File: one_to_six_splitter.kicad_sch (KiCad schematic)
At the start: 0 parts

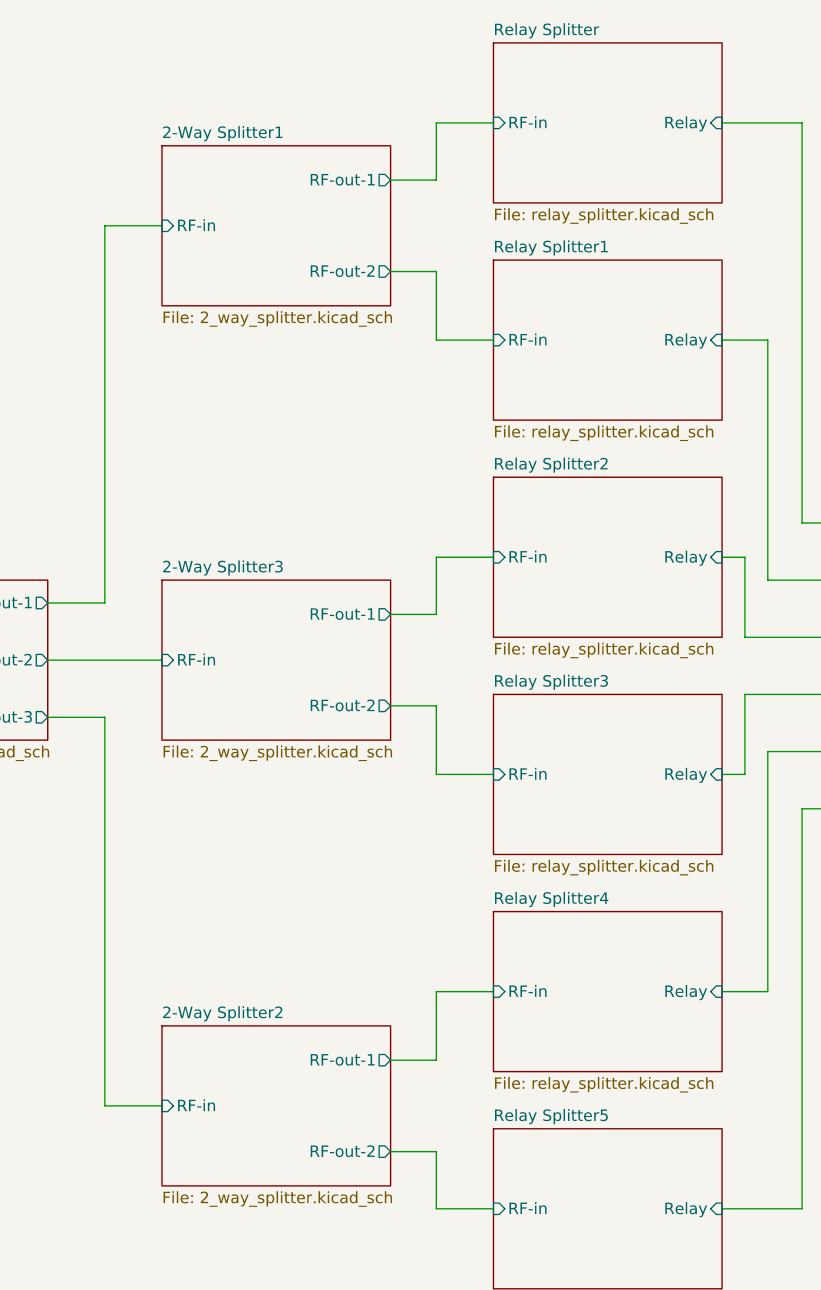
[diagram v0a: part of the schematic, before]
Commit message: changed to 1 to 6
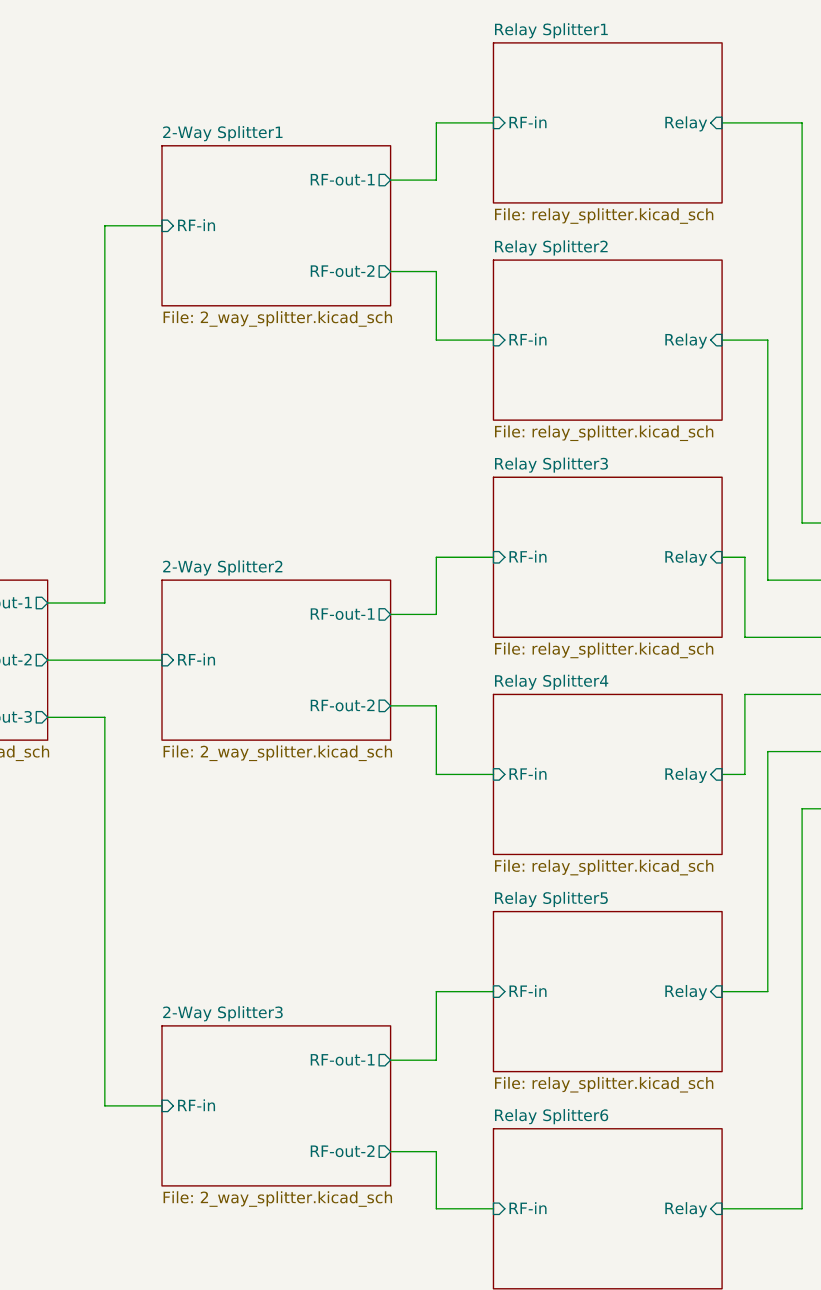
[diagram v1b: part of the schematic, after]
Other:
- removed sheet Relay Splitter
- added sheet Relay Splitter6 (relay_splitter.kicad_sch)
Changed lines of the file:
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@@
     (stroke (width 0.1524) (type solid) (color 0 0 0 0))
     (fill (color 0 0 0 0.0000))
-    (property "Sheet name" "Relay Splitter4" (id 0) (at 140.97 119.9384 0)
+    (property "Sheet name" "Relay Splitter5" (id 0) (at 140.97 119.9384 0)
       (effects (font (size 1.27 1.27)) (justify left bottom))
     )
@@
     (stroke (width 0.1524) (type solid) (color 0 0 0 0))
     (fill (color 0 0 0 0.0000))
-    (property "Sheet name" "Relay Splitter5" (id 0) (at 140.97 144.0684 0)
+    (property "Sheet name" "Relay Splitter6" (id 0) (at 140.97 144.0684 0)
       (effects (font (size 1.27 1.27)) (justify left bottom))
     )
@@
     (stroke (width 0.1524) (type solid) (color 0 0 0 0))
     (fill (color 0 0 0 0.0000))
-    (property "Sheet name" "Relay Splitter3" (id 0) (at 140.97 95.8084 0)
+    (property "Sheet name" "Relay Splitter4" (id 0) (at 140.97 95.8084 0)
       (effects (font (size 1.27 1.27)) (justify left bottom))
     )
@@
     (stroke (width 0.1524) (type solid) (color 0 0 0 0))
     (fill (color 0 0 0 0.0000))
-    (property "Sheet name" "Relay Splitter" (id 0) (at 140.97 23.4184 0)
+    (property "Sheet name" "Relay Splitter1" (id 0) (at 140.97 23.4184 0)
       (effects (font (size 1.27 1.27)) (justify left bottom))
     )
@@
     (stroke (width 0.1524) (type solid) (color 0 0 0 0))
     (fill (color 0 0 0 0.0000))
-    (property "Sheet name" "2-Way Splitter2" (id 0) (at 104.14 132.6384 0)
+    (property "Sheet name" "2-Way Splitter3" (id 0) (at 104.14 132.6384 0)
       (effects (font (size 1.27 1.27)) (justify left bottom))
     )
@@
     (stroke (width 0.1524) (type solid) (color 0 0 0 0))
     (fill (color 0 0 0 0.0000))
-    (property "Sheet name" "2-Way Splitter3" (id 0) (at 104.14 83.1084 0)
+    (property "Sheet name" "2-Way Splitter2" (id 0) (at 104.14 83.1084 0)
       (effects (font (size 1.27 1.27)) (justify left bottom))
     )
@@
     (stroke (width 0.1524) (type solid) (color 0 0 0 0))
     (fill (color 0 0 0 0.0000))
-    (property "Sheet name" "Relay Splitter1" (id 0) (at 140.97 47.5484 0)
+    (property "Sheet name" "Relay Splitter2" (id 0) (at 140.97 47.5484 0)
       (effects (font (size 1.27 1.27)) (justify left bottom))
     )
@@
     (stroke (width 0.1524) (type solid) (color 0 0 0 0))
     (fill (color 0 0 0 0.0000))
-    (property "Sheet name" "Relay Splitter2" (id 0) (at 140.97 71.6784 0)
+    (property "Sheet name" "Relay Splitter3" (id 0) (at 140.97 71.6784 0)
       (effects (font (size 1.27 1.27)) (justify left bottom))
     )

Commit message: pcb routed and made gerbers
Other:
- sheet Connectors ports: added RF-1, RF-2, RF-3, RF-4, RF-5, RF-6; removed none
- sheet Relay Splitter1 ports: added RF-out; removed none
- sheet Relay Splitter2 ports: added RF-out; removed none
- sheet Relay Splitter3 ports: added RF-out; removed none
- sheet Relay Splitter4 ports: added RF-out; removed none
- sheet Relay Splitter5 ports: added RF-out; removed none
- sheet Relay Splitter6 ports: added RF-out; removed none
